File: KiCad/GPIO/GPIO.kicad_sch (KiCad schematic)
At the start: 60 parts, among them J1 JTAG, J10 Conn_01x01, J11 TO_FP, J13 Conn_01x08, J14 Conn_01x08, J2 TO_BACKPLANE, J3 Conn_01x01, J4 Conn_01x01, J5 Conn_01x01, J7 Conn_01x04, J8 Conn_01x04, U1 EPM240T100, U10 SN74ALVC164245DGG, U11 SN74LV1T34DCK, U12 SN74LV1T34DCK, U13 SN74LV1T34DCK, U14 SN74LV1T34DCK, U2 MCP1319MT-29LE-OT, U20 SN74LV1T34DCK, U21 SN74LV1T34DCK, U22 SN74LV1T34DCK, U24 SN74LV1T34DCK, U25 74HCT244, U26 74HCT244, U27 SN74LV1T34DCK, U28 SN74LV1T34DCK, U3 W25Q32FVSS, U30 74HC574, U4 AMS1117-3.3, U5 74HC574, U6 74HCT244, U7 74HCT74, U8 SN74LV1T34DCK, U9 SN74LV1T34DCK

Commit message: Prepare for bring-up
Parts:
- added J16: Conn_01x04, Connector_PinHeader_2.54mm:PinHeader_1x04_P2.54mm_Vertical, symbol Connector_Generic:Conn_01x04
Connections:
- net +5V: now also J16.3 (Pin_3)
- net GND: now also J16.4 (Pin_4)
- net at U1.90 (IO2_90): now also J16.1 (Pin_1)
- net at U1.91 (IO2_91): now also J16.2 (Pin_2)

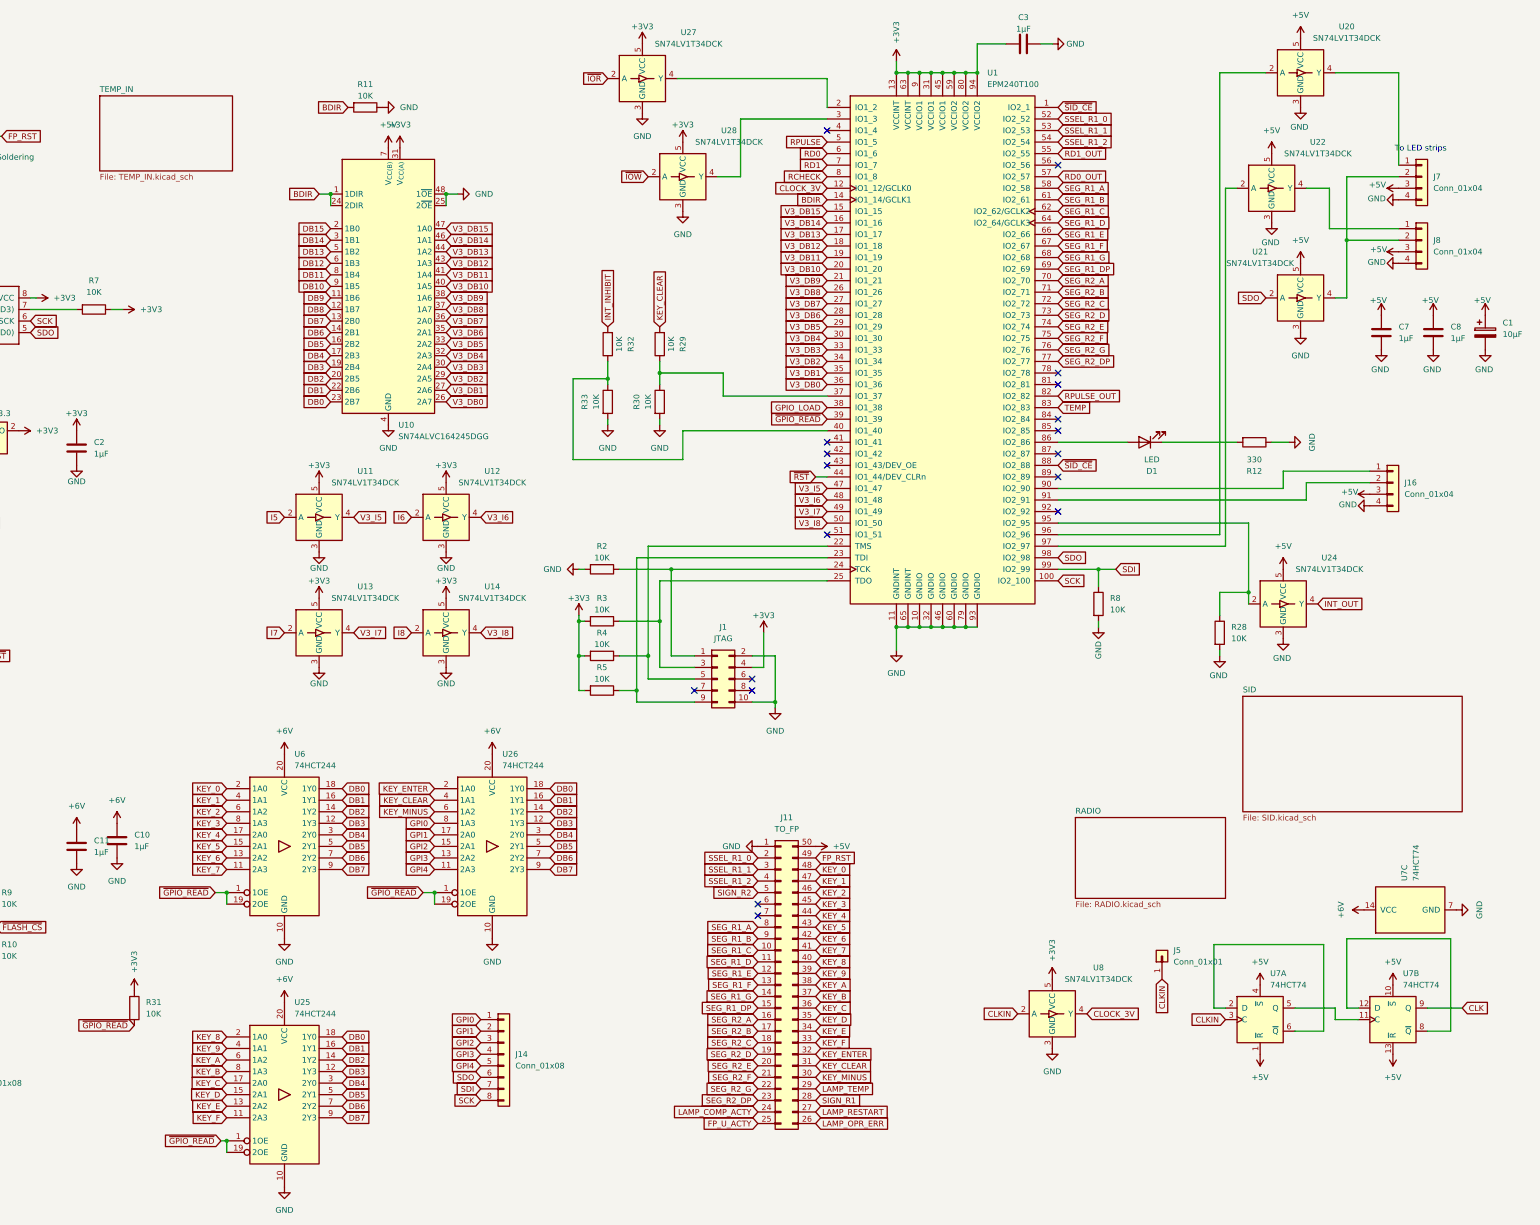
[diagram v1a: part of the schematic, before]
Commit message: Command handler done
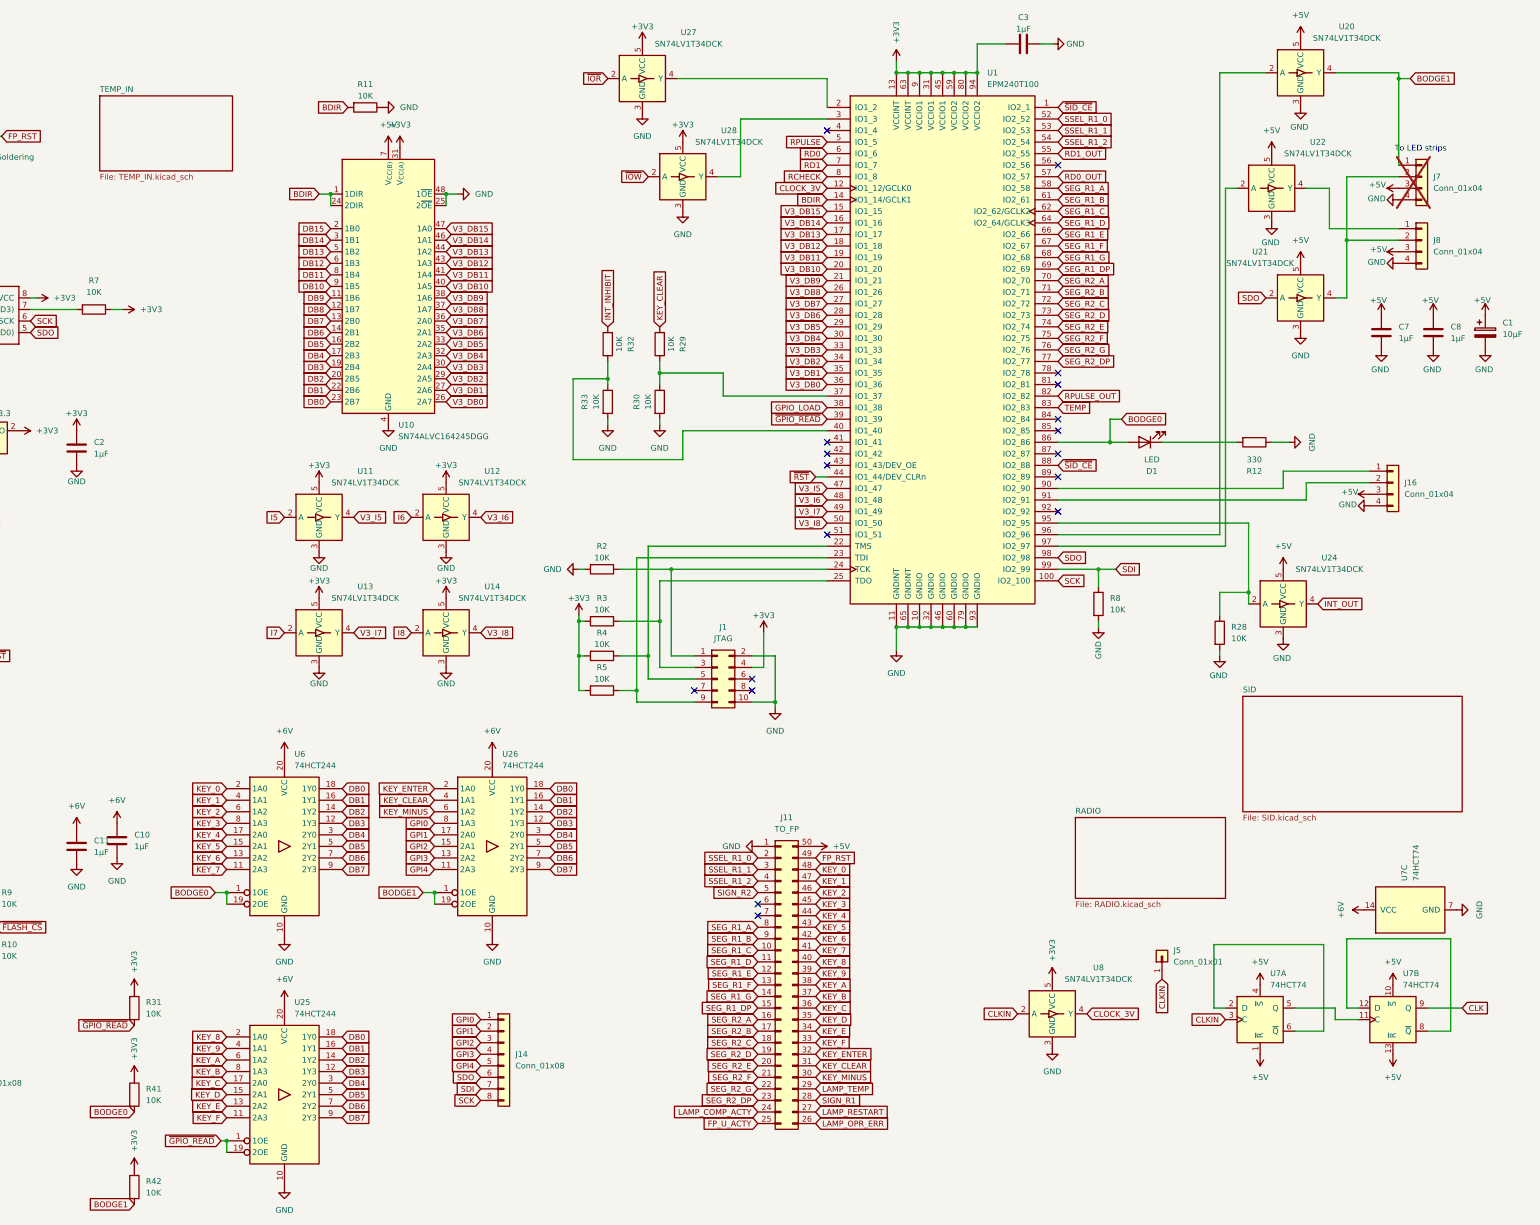
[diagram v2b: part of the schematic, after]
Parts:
- added R41, R42: 10K, Resistor_SMD:R_1206_3216Metric_Pad1.30x1.75mm_HandSolder, symbol Device:R
- J7: now not fitted
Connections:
- net +3V3: now also R41.1, R42.1
- net ~{GPIO_READ}: no longer U26.1 (1OE), U26.19 (2OE), U6.1 (1OE), U6.19 (2OE)
- net BODGE0: now reaches D1.2 (A), U1.86 (IO2_86)
- net BODGE0: now also U6.1 (1OE), U6.19 (2OE), R41.2
- net BODGE1: now reaches J7.1 (Pin_1), U20.4 (Y)
- net BODGE1: now also U26.1 (1OE), U26.19 (2OE), R42.2
